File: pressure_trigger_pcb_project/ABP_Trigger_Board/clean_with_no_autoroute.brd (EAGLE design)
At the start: 67 x 39.4 mm, 28 parts, among them U1 AD5206BRUZ10, U2 OPA4340UA

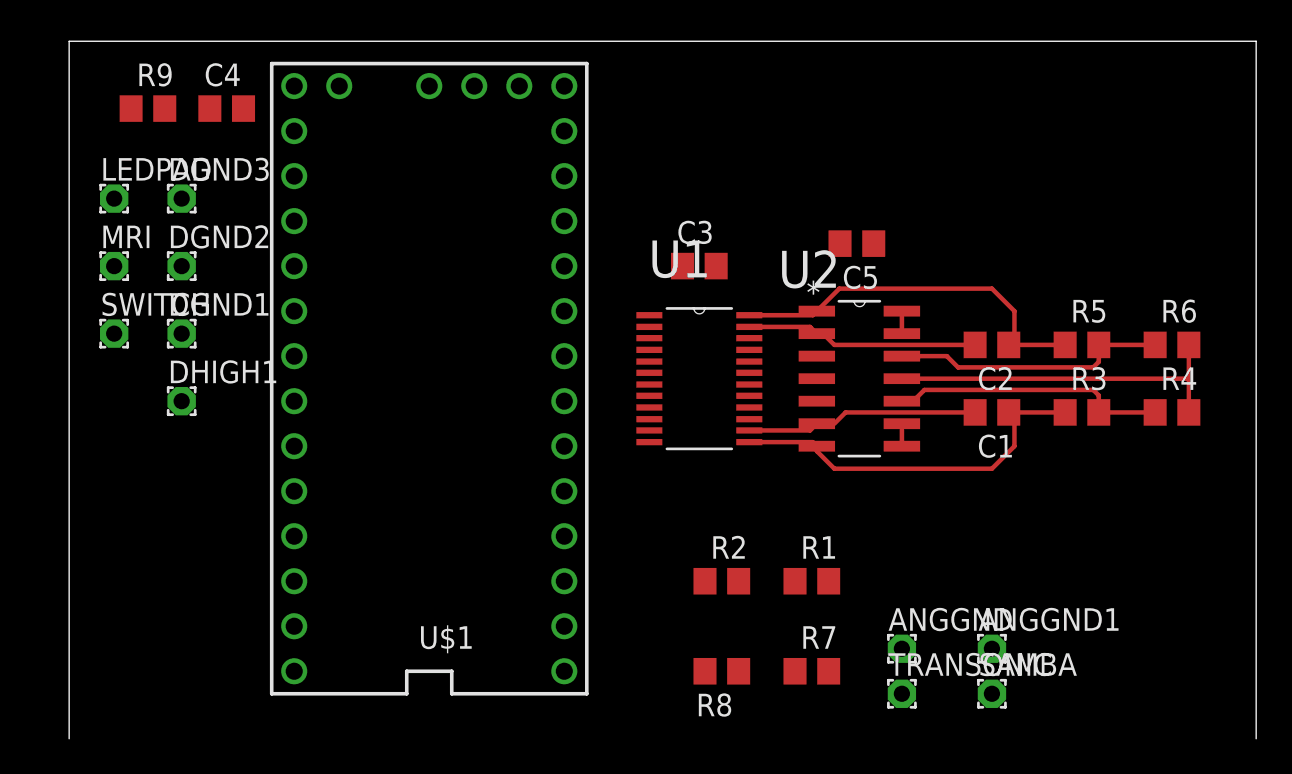
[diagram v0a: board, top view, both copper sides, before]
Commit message: routed REV A of the board, silkscreen not yet done
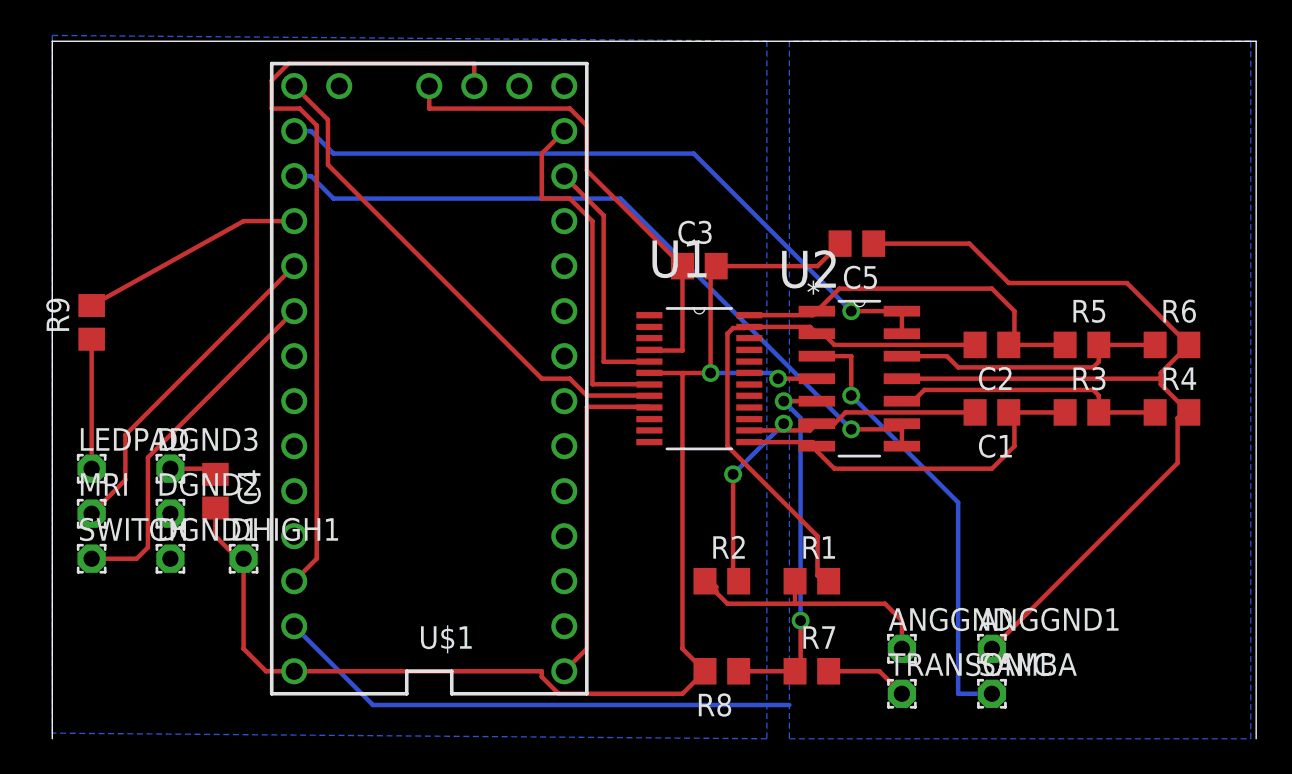
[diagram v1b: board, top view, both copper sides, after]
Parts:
- moved C4 21.6 mm to (8.26, 14.0), turned to 270 degrees
- moved LEDPAD 15.3 mm to (1.27, 15.2)
- moved DGND3 15.3 mm to (5.71, 15.2)
- moved MRI 14.0 mm to (1.27, 12.7)
- moved DGND2 14.0 mm to (5.71, 12.7)
- moved SWITCH 12.8 mm to (1.27, 10.2)
- moved DGND1 12.7 mm to (5.71, 10.2)
- moved R9 12.5 mm to (1.27, 23.5), turned to 90 degrees
- moved DHIGH1 9.55 mm to (9.84, 10.2)
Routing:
- net AGND: track 20.0 -> 103.2 mm
- net VCC: track 0.00 -> 77.4 mm, vias 0 -> 2
- net GND: track 0.00 -> 49.0 mm
- net 3.3V: track 0.00 -> 43.9 mm
- net N$2: track 1.27 -> 41.5 mm, vias 0 -> 1
- net N$1: track 1.27 -> 39.8 mm, vias 0 -> 1
- net N$19: track 0.00 -> 28.8 mm
- net N$10: track 0.00 -> 25.4 mm, vias 0 -> 1
- net N$4: track 0.00 -> 21.0 mm, vias 0 -> 2
- net N$16: track 0.00 -> 20.2 mm
- net N$8: track 0.00 -> 20.1 mm
- net N$15: track 0.00 -> 18.7 mm
- net N$3: track 12.8 -> 31.1 mm
- net N$7: track 0.00 -> 14.0 mm
- net N$14: track 0.00 -> 12.7 mm
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- added copper zone on layer 16, net AGND
- added copper zone on layer 16, net GND
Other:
- board size 67 x 39.4 mm -> 67.9 x 39.4 mm
